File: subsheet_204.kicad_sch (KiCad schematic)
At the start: 17 parts, among them J204 DB-25P Serial Port RS-232, U206 MC1488_QUAD_LINE_EIA-232D_DRI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, U207 MC1489_QUAD_LINE_EIA-232D_REC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

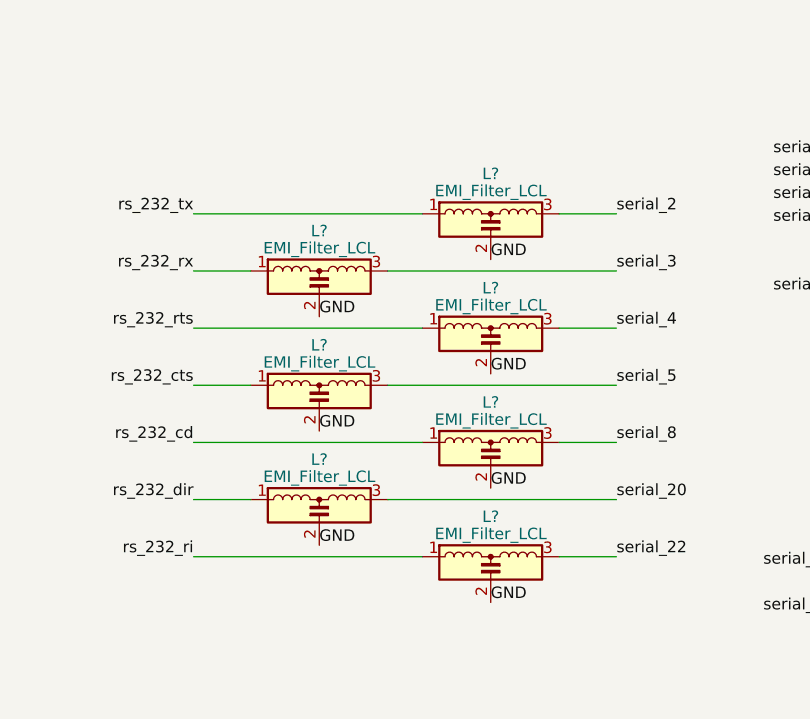
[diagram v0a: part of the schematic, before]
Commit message: Resolves #3 : [schematic] annotate video port with signal name
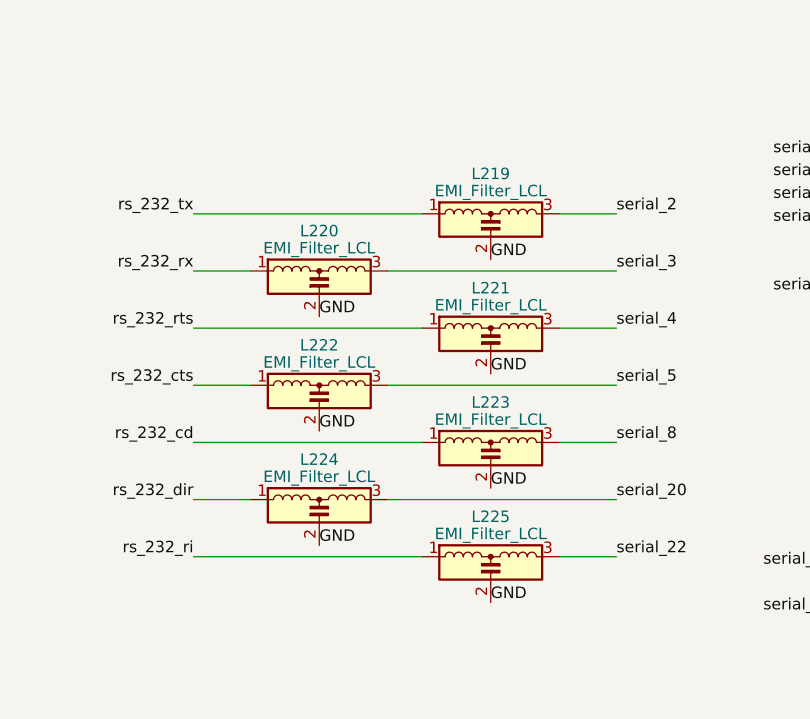
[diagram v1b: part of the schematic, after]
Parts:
- gave numbers to parts that had none: 7
